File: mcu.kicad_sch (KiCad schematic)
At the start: 54 parts, among them J10 PinHeader_2x10_P1.27mm_SMD_Sh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, SW5 SW_B3U-1000P_SMD, SW6 CAS-120TA, U1 STM32H753ZIT6, Y1 Resonator_32.768kHz_ECX-31B, Y2 Oscillator_25MHz_ESC_2016MV

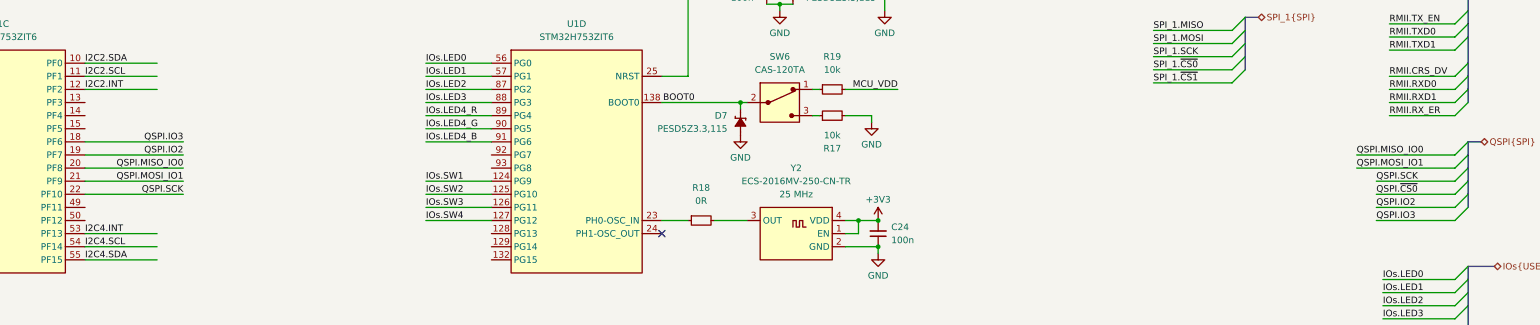
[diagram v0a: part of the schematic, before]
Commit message: [#94972] Reconnect QSPI to MCU
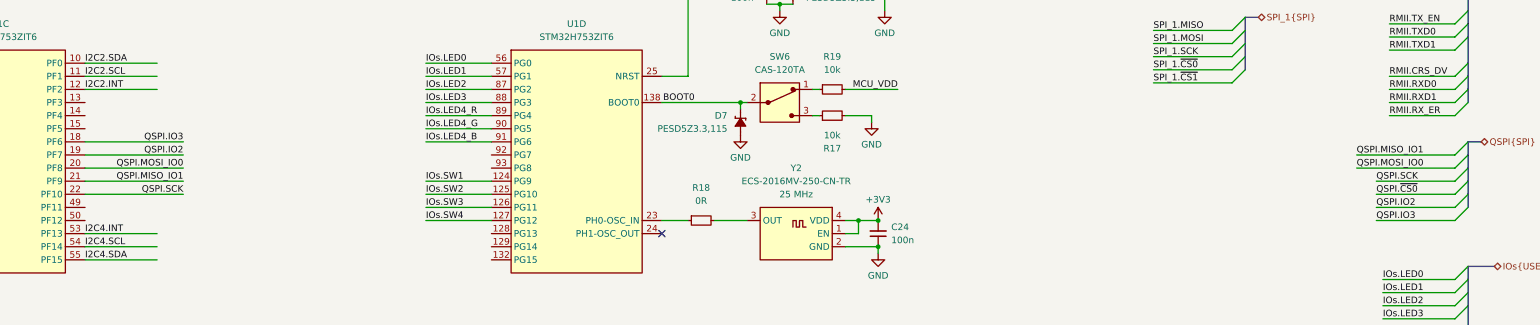
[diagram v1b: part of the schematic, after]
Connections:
- net QSPI.MISO_IO0 renamed QSPI.MOSI_IO0
- net QSPI.MOSI_IO1 renamed QSPI.MISO_IO1
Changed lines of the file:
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@@
 		)
 	)
-	(label "QSPI.MISO_IO0"
+	(label "QSPI.MISO_IO1"
 		(at 350.52 191.77 0)
 		(effects
@@
 		)
 	)
-	(label "QSPI.MISO_IO0"
-		(at 123.19 194.31 180)
+	(label "QSPI.MISO_IO1"
+		(at 123.19 196.85 180)
 		(effects
 			(font
@@
 		)
 	)
-	(label "QSPI.MOSI_IO1"
-		(at 123.19 196.85 180)
+	(label "QSPI.MOSI_IO0"
+		(at 123.19 194.31 180)
 		(effects
 			(font
@@
 		)
 	)
-	(label "QSPI.MOSI_IO1"
+	(label "QSPI.MOSI_IO0"
 		(at 350.52 194.31 0)
 		(effects

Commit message: [#95036] Manage I2C, UART, SPI interfaces for RPI and PMOD connectors
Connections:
- net IOs.SW4: no longer U1.127 (PG12)
- net UART_3.RTS: now also U1.74 (PB13); no longer U1.75 (PB14)
- net SPI_2.SCK: now reaches U1.117 (PD3)
- net SPI_2.~{CS0}: now reaches U1.26 (PC0)
- net SPI_2.MISO: now reaches U1.28 (PC2_C)
- net SPI_2.MOSI: now reaches U1.29 (PC3_C)
- net I2C3.SCL: now reaches U1.100 (PA8)
- net at R46.1: now also U1.127 (PG12); no longer U1.74 (PB13)
- net UART1.RX: now reaches U1.76 (PB15)
- net I2C_QWIIC.SDA renamed I2C3.SDA
- new net UART1.TX: U1.75 (PB14)
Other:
- note added: "TODO: Verify all UARTs RX/TX cross. Should I make one?"
- moved on the sheet: R41, R46

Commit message: [#95036] Add missing interfaces to MCU sheet
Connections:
- net ADC_CURRENT_IN: now reaches U1.49 (PF11)
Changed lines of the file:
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@@
 	(wire
 		(pts
-			(xy 138.43 91.44) (xy 149.86 91.44)
+			(xy 116.84 209.55) (xy 104.14 209.55)
 		)
 		(stroke
@@
 	(wire
 		(pts
-			(xy 226.06 204.47) (xy 232.41 204.47)
+			(xy 138.43 91.44) (xy 149.86 91.44)
 		)
 		(stroke
@@
 	(wire
 		(pts
-			(xy 358.14 110.49) (xy 369.57 110.49)
+			(xy 226.06 204.47) (xy 232.41 204.47)
 		)
 		(stroke
@@
 	(wire
 		(pts
-			(xy 220.98 176.53) (xy 215.9 176.53)
+			(xy 358.14 110.49) (xy 369.57 110.49)
 		)
 		(stroke
@@
 	(wire
 		(pts
-			(xy 198.12 58.42) (xy 198.12 59.69)
+			(xy 220.98 176.53) (xy 215.9 176.53)
 		)
 		(stroke
@@
 	(wire
 		(pts
-			(xy 104.14 212.09) (xy 118.11 212.09)
+			(xy 198.12 58.42) (xy 198.12 59.69)
 		)
 		(stroke
@@
 	(wire
 		(pts
+			(xy 104.14 207.01) (xy 116.84 207.01)
+		)
+		(stroke
+			(width 0)
+			(type default)
+		)
+	)
+	(wire
+		(pts
 			(xy 154.94 260.35) (xy 143.51 260.35)
 		)
@@
 		)
 	)
+	(wire
+		(pts
+			(xy 116.84 212.09) (xy 104.14 212.09)
+		)
+		(stroke
+			(width 0)
+			(type default)
+		)
+	)
 	(bus
 		(pts
@@
 	(wire
 		(pts
-			(xy 104.14 207.01) (xy 118.11 207.01)
-		)
-		(stroke
-			(width 0)
-			(type default)
-		)
-	)
-	(wire
-		(pts
 			(xy 222.25 21.59) (xy 236.22 21.59)
 		)
@@
 		)
 	)
+	(wire
+		(pts
+			(xy 104.14 201.93) (xy 107.95 201.93)
+		)
+		(stroke
+			(width 0)
+			(type default)
+		)
+	)
 	(bus
 		(pts
@@
 	(wire
 		(pts
-			(xy 104.14 209.55) (xy 118.11 209.55)
-		)
-		(stroke
-			(width 0)
-			(type default)
-		)
-	)
-	(wire
-		(pts
 			(xy 215.9 50.8) (xy 224.79 50.8)
 		)
@@
 	)
 	(label "I2C4.INT"
-		(at 104.14 207.01 0)
+		(at 116.84 207.01 180)
 		(effects
 			(font
 				(size 1.27 1.27)
 			)
-			(justify left bottom)
+			(justify right bottom)
 		)
 	)
@@
 	)
 	(label "I2C4.SDA"
-		(at 104.14 212.09 0)
+		(at 116.84 212.09 180)
 		(effects
 			(font
 				(size 1.27 1.27)
 			)
-			(justify left bottom)
+			(justify right bottom)
 		)
 	)
@@
 	)
 	(label "I2C4.SCL"
-		(at 104.14 209.55 0)
+		(at 116.84 209.55 180)
 		(effects
 			(font
 				(size 1.27 1.27)
 			)
-			(justify left bottom)
+			(justify right bottom)
 		)
 	)
@@
 		)
 	)
+	(hierarchical_label "ACC_GYRO_INT1"
+		(shape output)
+		(at 476.25 226.06 0)
+		(effects
+			(font
+				(size 1.27 1.27)
+			)
+			(justify left)
+		)
+	)
 	(hierarchical_label "JTAG{JTAG}"
 		(shape bidirectional)
@@
 		)
 	)
+	(hierarchical_label "~{FTDI_RESET}"
+		(shape output)
+		(at 478.79 217.17 0)
+		(effects
+			(font
+				(size 1.27 1.27)
+			)
+			(justify left)
+		)
+	)
 	(hierarchical_label "I2C2{I2C}"
 		(shape bidirectional)
@@
 		)
 	)
+	(hierarchical_label "ADC_CURRENT_IN"
+		(shape input)
+		(at 107.95 201.93 0)
+		(effects
+			(font
+				(size 1.27 1.27)
+				(thickness 0.1588)
+			)
+			(justify left)
+		)
+	)
 	(hierarchical_label "SPI_2{SPI}"
 		(shape bidirectional)
@@
 		)
 	)
+	(hierarchical_label "MAG_~{INT}"
+		(shape output)
+		(at 476.25 223.52 0)
+		(effects
+			(font
+				(size 1.27 1.27)
+			)
+			(justify left)
+		)
+	)
 	(hierarchical_label "GPIO[0..27]"
 		(shape bidirectional)
@@
 		(effects
 			(font
+				(size 1.27 1.27)
+			)
+			(justify left)
+		)
+	)
+	(hierarchical_label "ACC_GYRO_INT2"
+		(shape output)
+		(at 476.25 228.6 0)
+		(effects
+			(font

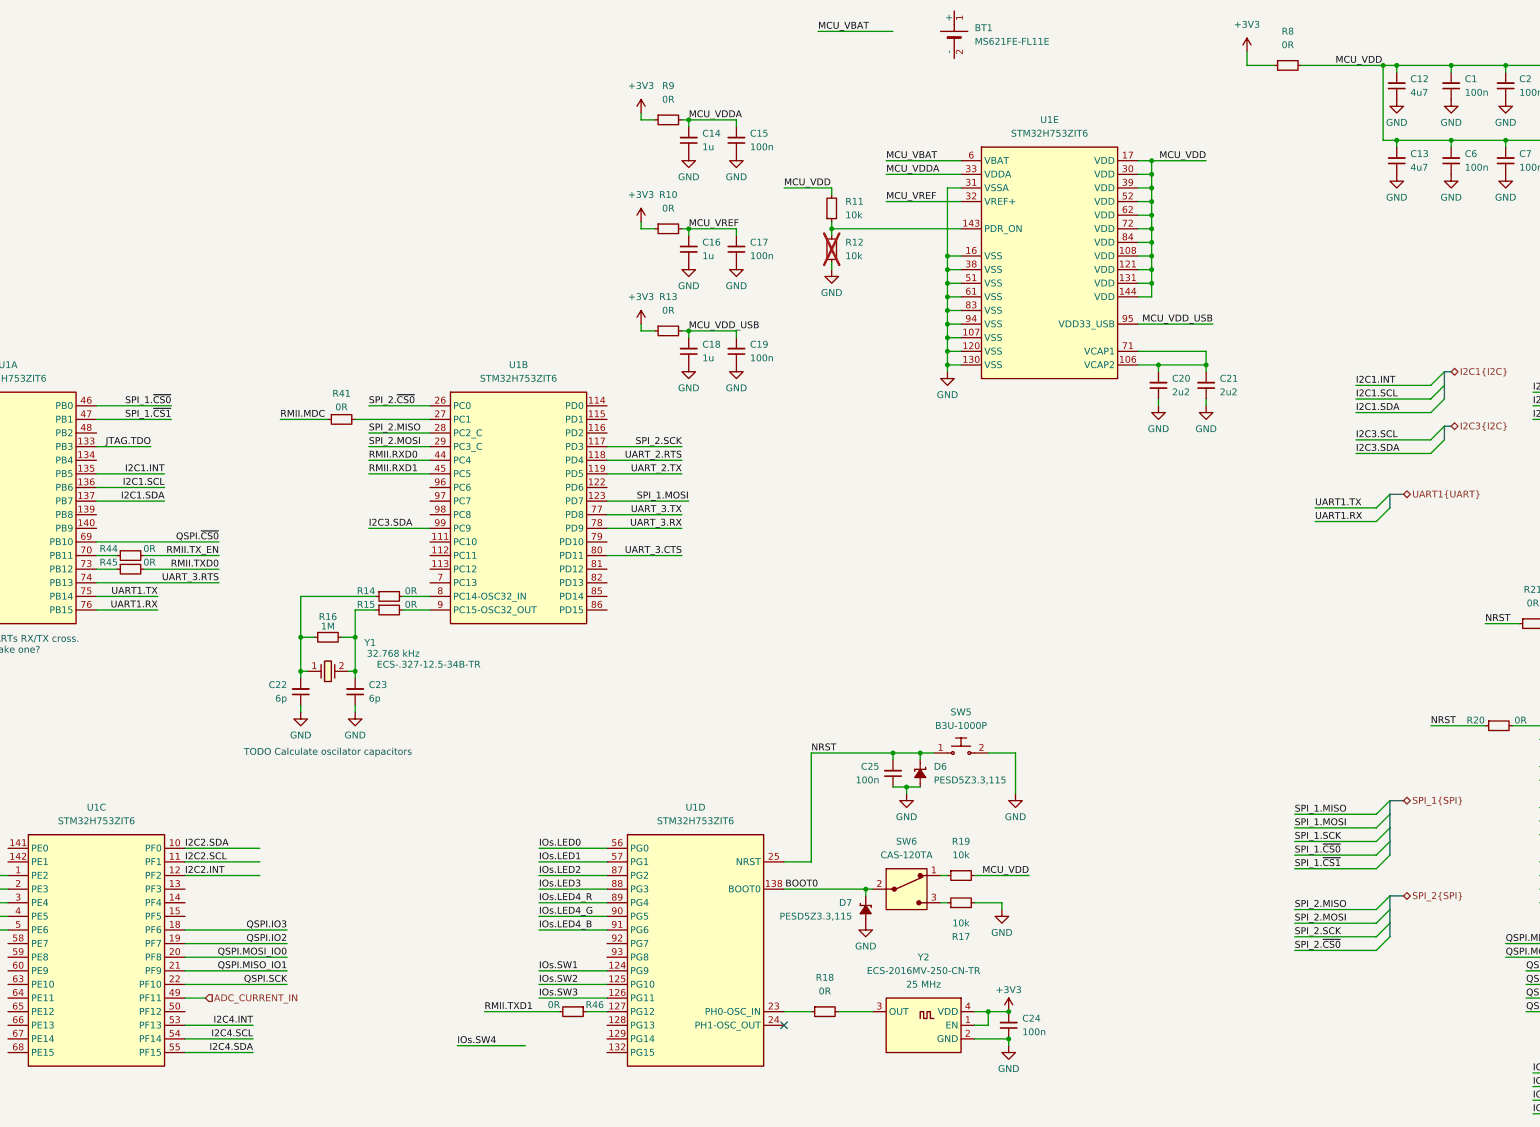
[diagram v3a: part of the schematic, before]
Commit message: [#95036] Add CAN bus placeholders
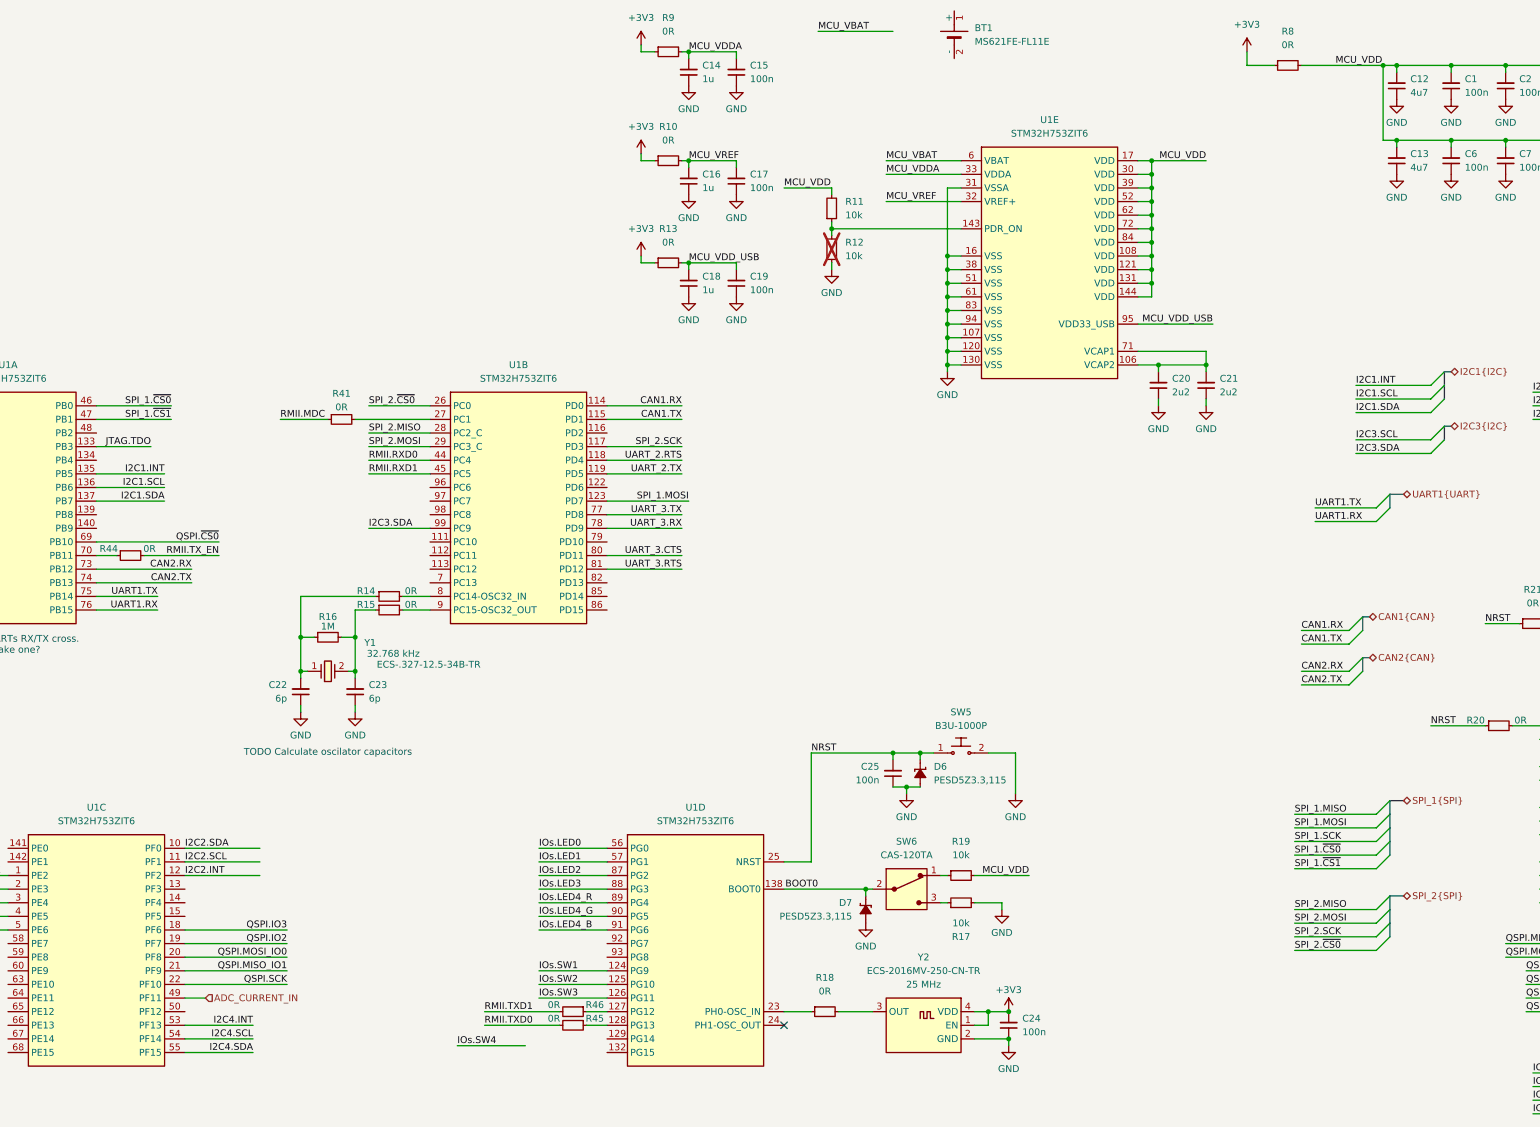
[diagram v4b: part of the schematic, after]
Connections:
- net UART_3.RTS: now also U1.81 (PD12); no longer U1.74 (PB13)
- net at U1.128 (PG13): now also R45.1
- net CAN1.RX: now reaches U1.114 (PD0)
- net CAN1.TX: now reaches U1.115 (PD1)
- net CAN2.RX: now reaches U1.73 (PB12)
- net CAN2.RX: no longer R45.1
- new net CAN2.TX: U1.74 (PB13)
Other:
- moved on the sheet: C14, C15, C16, C17, C18, C19, R10, R13, R45, R9

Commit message: [#95036] Start connecting RPI signals to MCU
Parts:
- removed R14: R_0R_0402, antmicro-footprints:R_0402_1005Metric, symbol antmicroResistors0402:R_0R_0402
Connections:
- net GPIO4: now also U1.96 (PC6)
- net at C22.2, R16.1, Y1.1: now also U1.8 (PC14-OSC32_IN)
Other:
- note added: "PC6 is SWPMI capable"

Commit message: [#95036] Connect PWM capable outputs of STM32
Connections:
- net GPIO12: now also U1.59 (PE8)
- net GPIO13: now also U1.63 (PE10)
- net GPIO18: now also U1.64 (PE11)
- net GPIO19: now also U1.67 (PE14)
- net IOs.LED0: now also U1.134 (PB4); no longer U1.56 (PG0)
- net IOs.LED1: now also U1.97 (PC7); no longer U1.57 (PG1)
- net IOs.LED2: now also U1.139 (PB8); no longer U1.87 (PG2)
- net IOs.LED3: now also U1.47 (PB1); no longer U1.88 (PG3)
- net IOs.LED4_B: now also U1.86 (PD15); no longer U1.91 (PG6)
- net IOs.LED4_G: now also U1.85 (PD14); no longer U1.90 (PG5)
- net IOs.LED4_R: now also U1.82 (PD13); no longer U1.89 (PG4)
- net IOs.SW1: now also U1.92 (PG7); no longer U1.124 (PG9)
- net IOs.SW2: now also U1.93 (PG8); no longer U1.125 (PG10)
- net IOs.SW3: now also U1.124 (PG9); no longer U1.126 (PG11)
- net IOs.SW4: now also U1.125 (PG10)
- net SPI_1.~{CS1}: now also U1.48 (PB2); no longer U1.47 (PB1)
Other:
- note added: "33"
- note added: "PWM capable"
- note added: "https://pinout.xyz/pinout/1_wire"
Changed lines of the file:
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@@
 		)
 	)
+	(text "https://pinout.xyz/pinout/1_wire"
+		(exclude_from_sim no)
+		(at 528.828 174.244 0)
+		(effects
+			(font
+				(size 1.27 1.27)
+			)
+		)
+	)
 	(text "TODO Calculate oscilator capacitors\n"
 		(exclude_from_sim no)
@@
 		)
 	)
+	(text "PWM capable"
+		(exclude_from_sim no)
+		(at 107.442 93.218 0)
+		(effects
+			(font
+				(size 1.27 1.27)
+			)
+		)
+	)
+	(text "33\n\n"
+		(exclude_from_sim no)
+		(at 508.508 83.566 0)
+		(effects
+			(font
+				(size 1.27 1.27)
+			)
+		)
+	)
 	(text "JTAG/TRACE Connector"
 		(exclude_from_sim no)
@@
 		)
 	)
+	(text "PWM capable"
+		(exclude_from_sim no)
+		(at 107.442 110.998 0)
+		(effects
+			(font
+				(size 1.27 1.27)
+			)
+		)
+	)
+	(text "PWM capable"
+		(exclude_from_sim no)
+		(at 52.832 193.548 0)
+		(effects
+			(font
+				(size 1.27 1.27)
+			)
+		)
+	)
+	(text "PWM capable"
+		(exclude_from_sim no)
+		(at 107.442 100.838 0)
+		(effects
+			(font
+				(size 1.27 1.27)
+			)
+		)
+	)
+	(text "PWM capable"
+		(exclude_from_sim no)
+		(at 52.832 208.788 0)
+		(effects
+			(font
+				(size 1.27 1.27)
+			)
+		)
+	)
+	(text "PWM capable"
+		(exclude_from_sim no)
+		(at 52.832 198.628 0)
+		(effects
+			(font
+				(size 1.27 1.27)
+			)
+		)
+	)
+	(text "PWM capable"
+		(exclude_from_sim no)
+		(at 131.572 108.458 0)
+		(effects
+			(font
+				(size 1.27 1.27)
+			)
+		)
+	)
+	(text "PWM capable"
+		(exclude_from_sim no)
+		(at 52.832 201.168 0)
+		(effects
+			(font
+				(size 1.27 1.27)
+			)
+		)
+	)
 	(junction
 		(at 284.48 45.72)
@@
 	(wire
 		(pts
-			(xy 101.6 93.98) (xy 87.63 93.98)
+			(xy 101.6 96.52) (xy 87.63 96.52)
 		)
 		(stroke
@@
 	(wire
 		(pts
-			(xy 170.18 173.99) (xy 182.88 173.99)
+			(xy 100.33 101.6) (xy 87.63 101.6)
 		)
 		(stroke
@@
 	(wire
 		(pts
-			(xy 170.18 181.61) (xy 182.88 181.61)
+			(xy 100.33 93.98) (xy 87.63 93.98)
 		)
 		(stroke
@@
 	(wire
 		(pts
+			(xy 59.69 209.55) (xy 71.12 209.55)
+		)
+		(stroke
+			(width 0)
+			(type default)
+		)
+	)
+	(wire
+		(pts
 			(xy 44.45 114.3) (xy 54.61 114.3)
 		)
@@
 	(wire
 		(pts
+			(xy 59.69 201.93) (xy 71.12 201.93)
+		)
+		(stroke
+			(width 0)
+			(type default)
+		)
+	)
+	(wire
+		(pts
 			(xy 133.35 262.89) (xy 132.08 262.89)
 		)
@@
 	(wire
 		(pts
-			(xy 170.18 196.85) (xy 182.88 196.85)
+			(xy 170.18 191.77) (xy 182.88 191.77)
 		)
 		(stroke
@@
 	(wire
 		(pts
-			(xy 170.18 201.93) (xy 182.88 201.93)
+			(xy 170.18 196.85) (xy 182.88 196.85)
 		)
 		(stroke
@@
 	(wire
 		(pts
+			(xy 59.69 199.39) (xy 71.12 199.39)
+		)
+		(stroke
+			(width 0)
+			(type default)
+		)
+	)
+	(wire
+		(pts
 			(xy 59.69 184.15) (xy 71.12 184.15)
 		)
@@
 	(wire
 		(pts
+			(xy 71.12 194.31) (xy 59.69 194.31)
+		)
+		(stroke
+			(width 0)
+			(type default)
+		)
+	)
+	(wire
+		(pts
 			(xy 246.38 66.04) (xy 248.92 66.04)
 		)
@@
 	(wire
 		(pts
-			(xy 182.88 184.15) (xy 170.18 184.15)
+			(xy 182.88 124.46) (xy 195.58 124.46)
 		)
 		(stroke
@@
 	(wire
 		(pts
-			(xy 154.94 210.82) (xy 167.64 210.82)
+			(xy 170.18 199.39) (xy 182.88 199.39)
 		)
 		(stroke
@@
 	(wire
 		(pts
-			(xy 170.18 176.53) (xy 182.88 176.53)
+			(xy 138.43 109.22) (xy 149.86 109.22)
 		)
 		(stroke
@@
 	(wire
 		(pts
-			(xy 182.88 189.23) (xy 170.18 189.23)
+			(xy 195.58 129.54) (xy 182.88 129.54)
 		)
 		(stroke
@@
 	(wire
 		(pts
-			(xy 170.18 199.39) (xy 182.88 199.39)
+			(xy 170.18 194.31) (xy 182.88 194.31)
 		)
 		(stroke
@@
 	(wire
 		(pts
-			(xy 182.88 186.69) (xy 170.18 186.69)
+			(xy 182.88 127) (xy 195.58 127)
 		)
 		(stroke
@@
 	(wire
 		(pts
-			(xy 170.18 179.07) (xy 182.88 179.07)
+			(xy 100.33 111.76) (xy 87.63 111.76)
 		)
 		(stroke
@@
 	)
 	(label "GPIO19"
-		(at 474.98 152.4 0)
+		(at 59.69 209.55 0)
 		(effects
 			(font
@@
 	)
 	(label "IOs.SW4"
-		(at 154.94 210.82 0)
+		(at 170.18 199.39 0)
 		(effects
 			(font
@@
 	)
 	(label "IOs.SW1"
-		(at 170.18 196.85 0)
+		(at 170.18 191.77 0)
 		(effects
 			(font
@@
 	)
 	(label "IOs.LED1"
-		(at 170.18 176.53 0)
+		(at 138.43 109.22 0)
 		(effects
 			(font
@@
 	)
 	(label "GPIO13"
-		(at 474.98 142.24 0)
+		(at 59.69 199.39 0)
 		(effects
 			(font
@@
 	)
 	(label "GPIO18"
-		(at 474.98 149.86 0)
+		(at 59.69 201.93 0)
 		(effects
 			(font
@@
 	)
 	(label "IOs.SW2"
-		(at 170.18 199.39 0)
+		(at 170.18 194.31 0)
 		(effects
 			(font
@@
 	)
 	(label "SPI_1.~{CS1}"
-		(at 101.6 93.98 180)
+		(at 101.6 96.52 180)
 		(effects
 			(font
@@
 	)
 	(label "IOs.LED4_B"
-		(at 170.18 189.23 0)
+		(at 195.58 129.54 180)
 		(effects
 			(font
 				(size 1.27 1.27)
 			)
-			(justify left bottom)
+			(justify right bottom)
 		)
 	)
 	(label "IOs.LED0"
-		(at 170.18 173.99 0)
+		(at 100.33 101.6 180)
 		(effects
 			(font
 				(size 1.27 1.27)
 			)
-			(justify left bottom)
+			(justify right bottom)
 		)
 	)
 	(label "IOs.LED4_R"
-		(at 170.18 184.15 0)
+		(at 195.58 124.46 180)
 		(effects
 			(font
 				(size 1.27 1.27)
 			)
-			(justify left bottom)
+			(justify right bottom)
 		)
 	)
@@
 	)
 	(label "GPIO12"
-		(at 474.98 139.7 0)
+		(at 59.69 194.31 0)
 		(effects
 			(font
@@
 	)
 	(label "IOs.SW3"
-		(at 170.18 201.93 0)
+		(at 170.18 196.85 0)
 		(effects
 			(font
@@
 	)
 	(label "IOs.LED2"
-		(at 170.18 179.07 0)
+		(at 100.33 111.76 180)
 		(effects
 			(font
 				(size 1.27 1.27)
 			)
-			(justify left bottom)
+			(justify right bottom)
 		)
 	)
@@
 	)
 	(label "IOs.LED4_G"
-		(at 170.18 186.69 0)
+		(at 195.58 127 180)
 		(effects
 			(font
 				(size 1.27 1.27)
 			)
-			(justify left bottom)
+			(justify right bottom)
 		)
 	)
@@
 	)
 	(label "IOs.LED3"
-		(at 170.18 181.61 0)
+		(at 100.33 93.98 180)
 		(effects
 			(font
 				(size 1.27 1.27)
 			)
-			(justify left bottom)
+			(justify right bottom)
 		)
 	)

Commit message: [#95036] Connect PMOD pins to MCU
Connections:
- net GPIO12: now also U1.60 (PE9); no longer U1.59 (PE8)
- net GPIO13: now also U1.64 (PE11); no longer U1.63 (PE10)
- net GPIO18: now also U1.66 (PE13); no longer U1.64 (PE11)
- net IOs.LED2: now also U1.98 (PC8); no longer U1.139 (PB8)
- net PMOD1_IO5: now also U1.139 (PB8)
- net PMOD1_IO6: now also U1.129 (PG14)
- net PMOD1_IO7: now also U1.132 (PG15)
- net PMOD1_IO8: now also U1.140 (PB9)
- net PMOD2_IO5: now also U1.90 (PG5)
- net PMOD2_IO6: now also U1.46 (PB0), U1.91 (PG6)
- net SPI_1.~{CS0}: now also U1.111 (PC10); no longer U1.46 (PB0)
- net SPI_1.~{CS1}: now also U1.112 (PC11); no longer U1.48 (PB2)
- net SPI_1.MISO renamed SPI_1.MISO_IO1
- net SPI_1.MOSI renamed SPI_1.MOSI_IO0
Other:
- moved on the sheet: R45, R46
